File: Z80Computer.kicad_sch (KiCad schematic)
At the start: 41 parts, among them IC1 Z80CPU, IC2_EEPROM1 28C256, IC6_SRAM1 KM62256CLP, J1 Conn_Coaxial_Power, J2 Conn_01x08_Pin, J3 Conn_01x08_Pin, J4 Conn_01x40_Pin, SW1 SW_Push, U1 74LS244, U2 74LS32, U3 74LS273, U4 74LS138, U5 74LS00, U7 74LS00, X1 CXO_DIP14

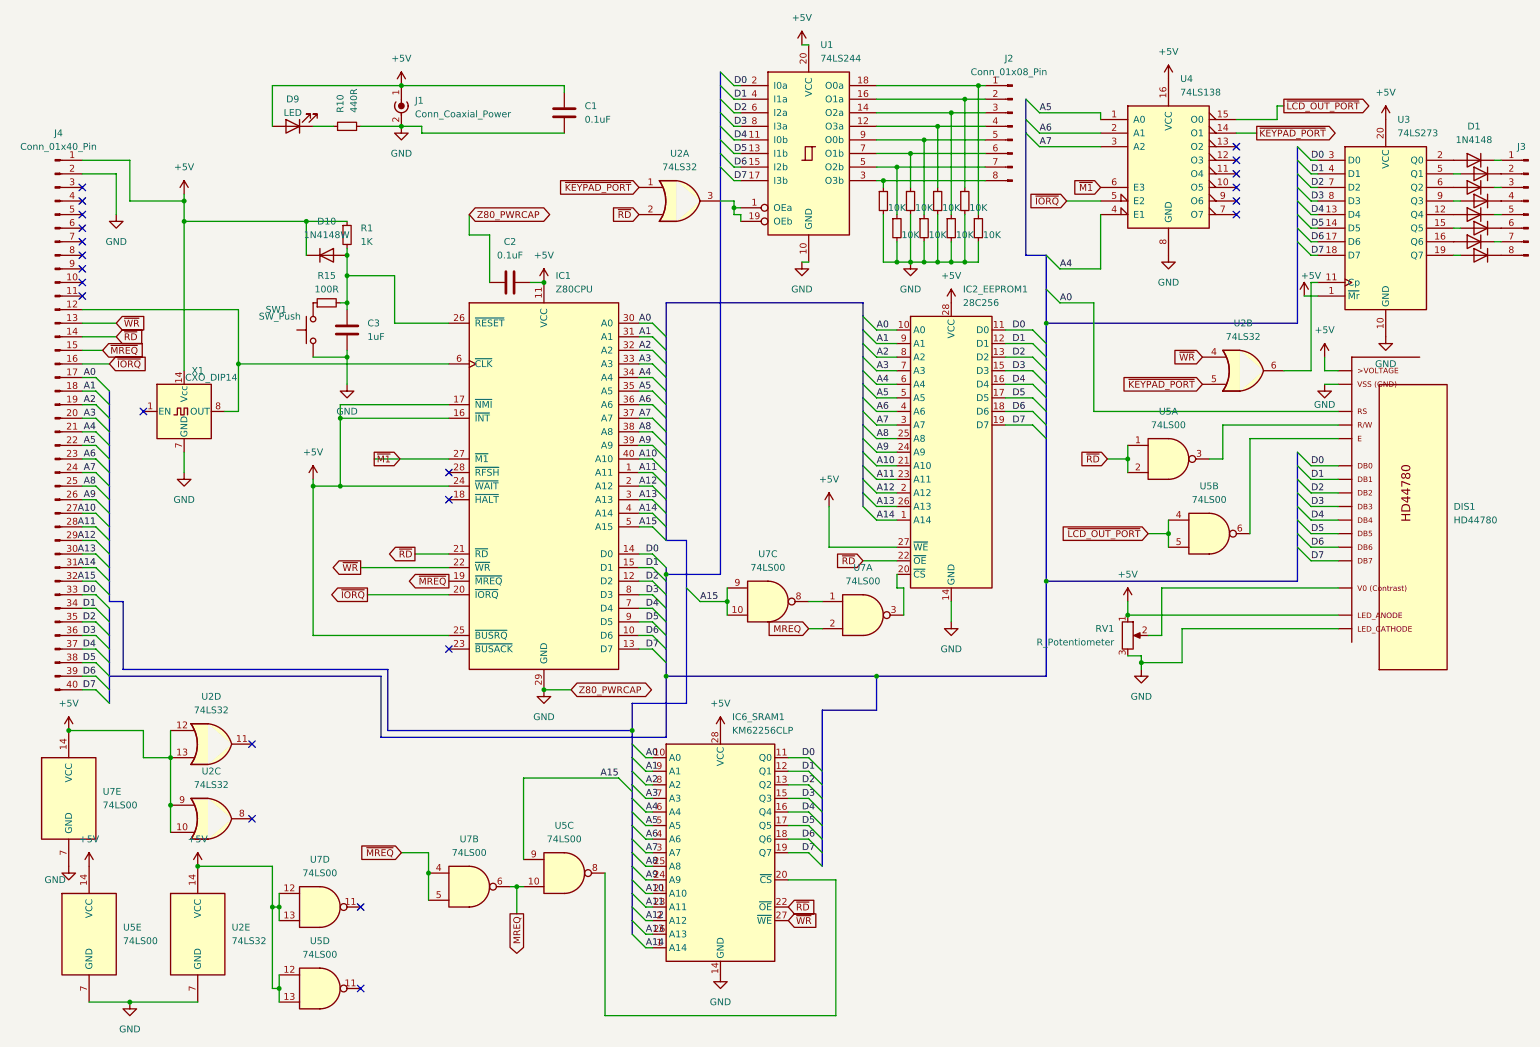
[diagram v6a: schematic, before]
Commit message: fixes for schematic (not redone PCB layout though
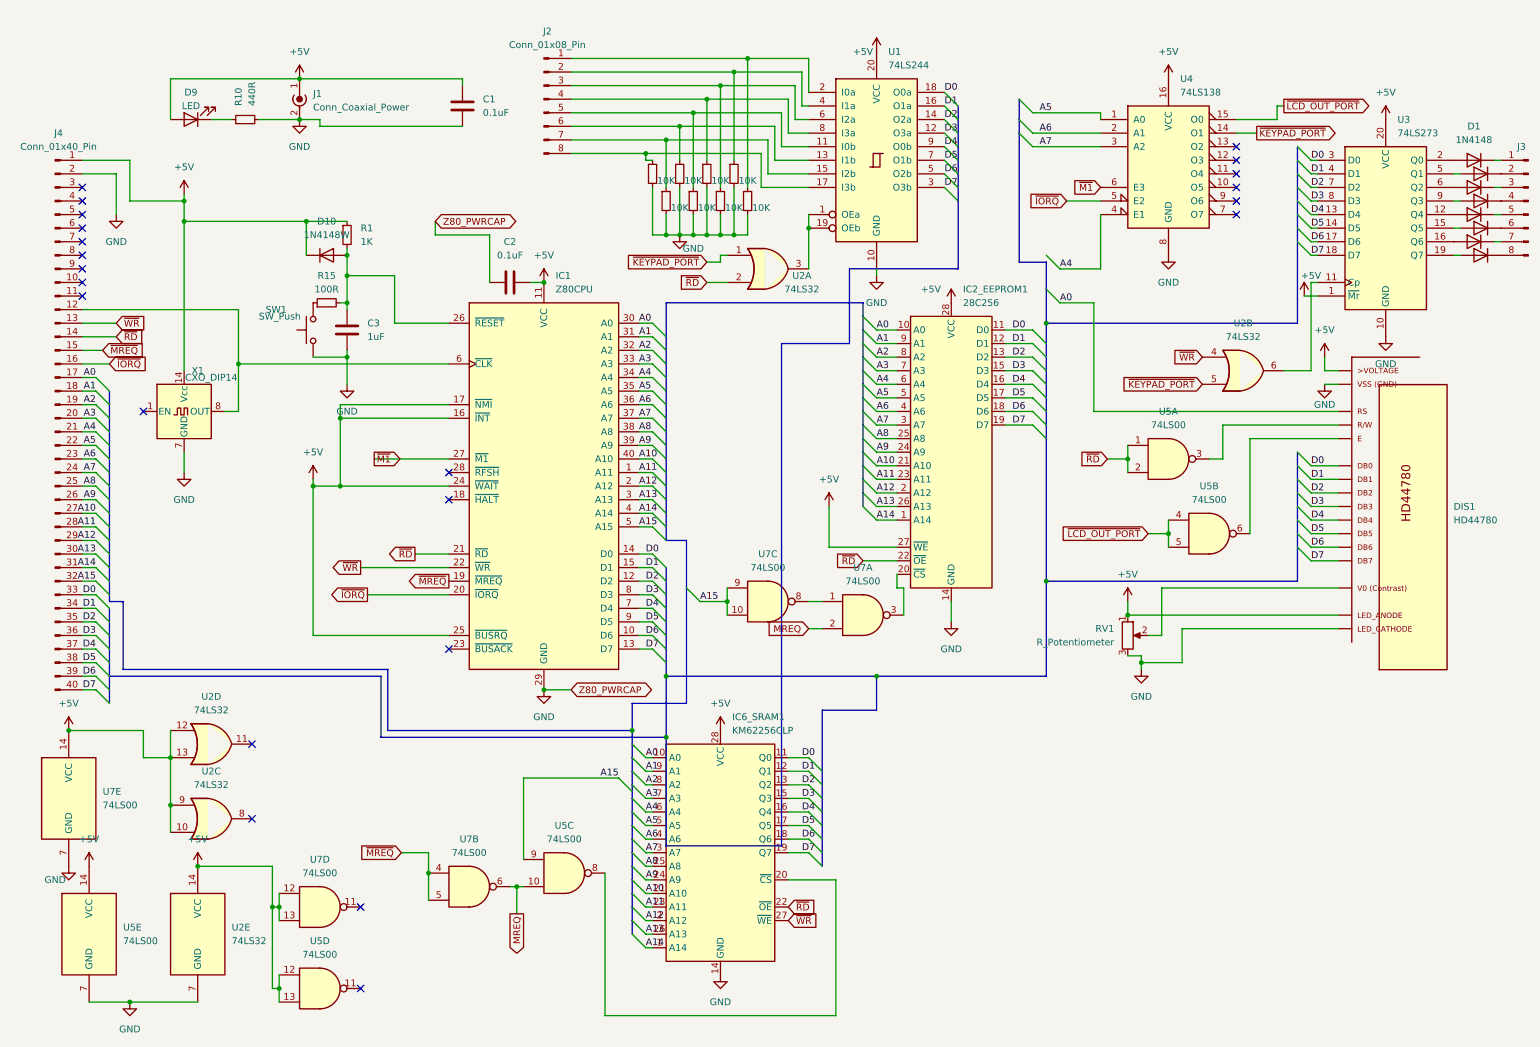
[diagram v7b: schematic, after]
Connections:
- net D0: now also U1.18 (O0a); no longer U1.2 (I0a)
- net D1: now also U1.16 (O1a); no longer U1.4 (I1a)
- net D2: now also U1.14 (O2a); no longer U1.6 (I2a)
- net D3: now also U1.12 (O3a); no longer U1.8 (I3a)
- net D4: now also U1.9 (O0b); no longer U1.11 (I0b)
- net D5: now also U1.7 (O1b); no longer U1.13 (I1b)
- net D6: now also U1.5 (O2b); no longer U1.15 (I2b)
- net D7: now also U1.3 (O3b); no longer U1.17 (I3b)
- net at J2.3 (Pin_3), R7.1: now also U1.6 (I2a); no longer U1.14 (O2a)
- net at J2.2 (Pin_2), R8.1: now also U1.4 (I1a); no longer U1.16 (O1a)
- net at J2.5 (Pin_5), R5.1: now also U1.11 (I0b); no longer U1.9 (O0b)
- net at J2.8 (Pin_8), R2.1: now also U1.17 (I3b); no longer U1.3 (O3b)
- net at J2.7 (Pin_7), R4.1: now also U1.15 (I2b); no longer U1.5 (O2b)
- net at J2.1 (Pin_1), R9.1: now also U1.2 (I0a); no longer U1.18 (O0a)
- net at J2.4 (Pin_4), R6.1: now also U1.8 (I3a); no longer U1.12 (O3a)
- net at J2.6 (Pin_6), R3.1: now also U1.13 (I1b); no longer U1.7 (O1b)
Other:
- moved on the sheet: C1, D9, J1, J2, R10, U1, U2A
